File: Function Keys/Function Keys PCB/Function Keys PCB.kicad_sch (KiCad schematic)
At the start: 30 parts, among them J1 Conn_01x05_Female, J2 Conn_01x05_Male

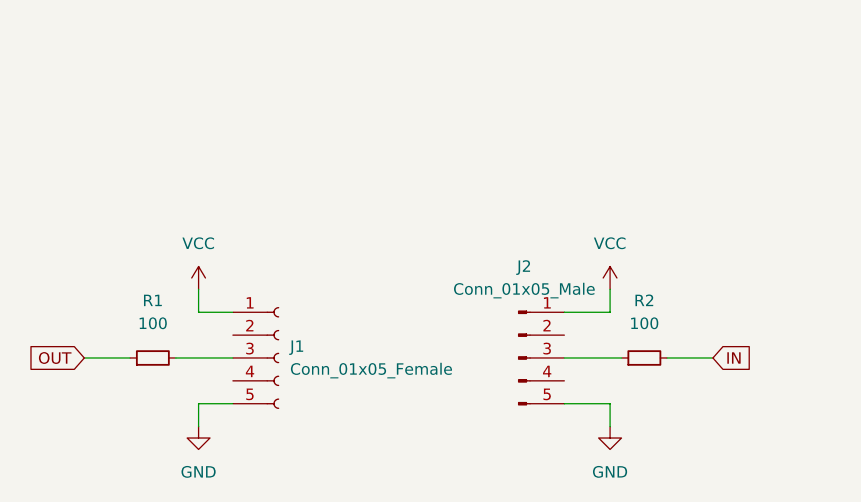
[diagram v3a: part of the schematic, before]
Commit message: Updated connectors
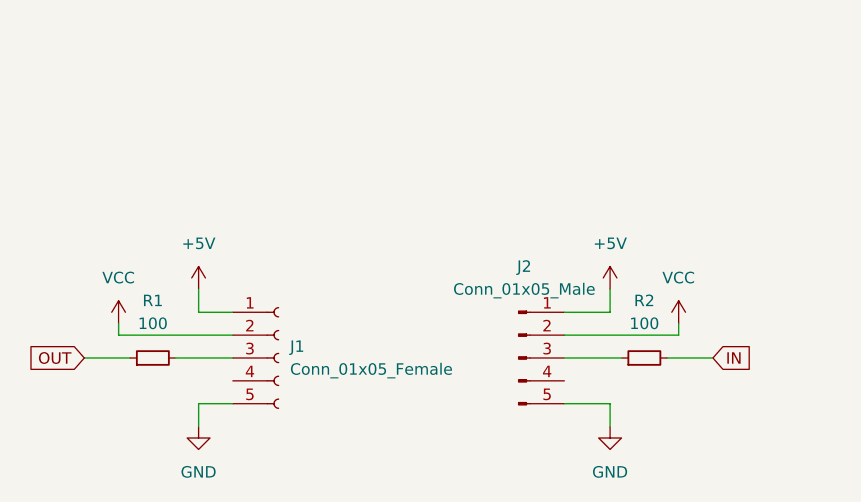
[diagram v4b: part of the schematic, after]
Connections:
- net VCC: now also J1.2 (Pin_2), J2.2 (Pin_2); no longer J1.1 (Pin_1), J2.1 (Pin_1)
- new net +5V: J1.1 (Pin_1), J2.1 (Pin_1)
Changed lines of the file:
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@@
+    (stroke (width 0) (type default) (color 0 0 0 0))
+  )
+  (wire (pts (xy 132.08 133.35) (xy 132.08 134.62))
     (stroke (width 0) (type default) (color 0 0 0 0))
   )
@@
     (stroke (width 0) (type default) (color 0 0 0 0))
   )
+  (wire (pts (xy 119.38 134.62) (xy 132.08 134.62))
+    (stroke (width 0) (type default) (color 0 0 0 0))
+  )
   (wire (pts (xy 176.53 73.66) (xy 176.53 74.93))
     (stroke (width 0) (type default) (color 0 0 0 0))
@@
     (stroke (width 0) (type default) (color 0 0 0 0))
   )
+  (wire (pts (xy 82.55 134.62) (xy 69.85 134.62))
+    (stroke (width 0) (type default) (color 0 0 0 0))
+  )
   (wire (pts (xy 85.09 73.66) (xy 85.09 74.93))
     (stroke (width 0) (type default) (color 0 0 0 0))
@@
   )
   (wire (pts (xy 193.04 72.39) (xy 193.04 73.66))
+    (stroke (width 0) (type default) (color 0 0 0 0))
+  )
+  (wire (pts (xy 69.85 134.62) (xy 69.85 133.35))
     (stroke (width 0) (type default) (color 0 0 0 0))
   )
@@
     (pin "2")
   )
+  (symbol (lib_id "power:+5V") (at 124.46 129.54 0) (unit 1)
+    (in_bom yes) (on_board yes) (fields_autoplaced)
+    (property "Reference" "#PWR?" (id 0) (at 124.46 133.35 0)
+      (effects (font (size 1.27 1.27)) hide)
+    )
+    (property "Value" "+5V" (id 1) (at 124.46 124.46 0))
+    (property "Footprint" "" (id 2) (at 124.46 129.54 0)
+      (effects (font (size 1.27 1.27)) hide)
+    )
+    (property "Datasheet" "" (id 3) (at 124.46 129.54 0)
+      (effects (font (size 1.27 1.27)) hide)
+    )
+    (pin "1")
+  )
   (symbol (lib_id "Connector:Conn_01x05_Male") (at 114.3 137.16 0) (unit 1)
     (in_bom yes) (on_board yes) (fields_autoplaced)
@@
     (pin "2")
   )
+  (symbol (lib_id "power:+5V") (at 78.74 129.54 0) (unit 1)
+    (in_bom yes) (on_board yes) (fields_autoplaced)
+    (property "Reference" "#PWR?" (id 0) (at 78.74 133.35 0)
+      (effects (font (size 1.27 1.27)) hide)
+    )
+    (property "Value" "+5V" (id 1) (at 78.74 124.46 0))
+    (property "Footprint" "" (id 2) (at 78.74 129.54 0)
+      (effects (font (size 1.27 1.27)) hide)
+    )
+    (property "Datasheet" "" (id 3) (at 78.74 129.54 0)
+      (effects (font (size 1.27 1.27)) hide)
+    )
+    (pin "1")
+  )
   (symbol (lib_id "MX_Alps_Hybrid:MX-NoLED") (at 114.3 68.58 0) (unit 1)
     (in_bom yes) (on_board yes) (fields_autoplaced)
@@
     (pin "1")
   )
-  (symbol (lib_id "power:VCC") (at 124.46 129.54 0) (unit 1)
-    (in_bom yes) (on_board yes) (fields_autoplaced)
-    (property "Reference" "#PWR0103" (id 0) (at 124.46 133.35 0)
-      (effects (font (size 1.27 1.27)) hide)
-    )
-    (property "Value" "VCC" (id 1) (at 124.46 124.46 0))
-    (property "Footprint" "" (id 2) (at 124.46 129.54 0)
-      (effects (font (size 1.27 1.27)) hide)
-    )
-    (property "Datasheet" "" (id 3) (at 124.46 129.54 0)
+  (symbol (lib_id "power:VCC") (at 132.08 133.35 0) (unit 1)
+    (in_bom yes) (on_board yes) (fields_autoplaced)
+    (property "Reference" "#PWR0103" (id 0) (at 132.08 137.16 0)
+      (effects (font (size 1.27 1.27)) hide)
+    )
+    (property "Value" "VCC" (id 1) (at 132.08 128.27 0))
+    (property "Footprint" "" (id 2) (at 132.08 133.35 0)
+      (effects (font (size 1.27 1.27)) hide)
+    )
+    (property "Datasheet" "" (id 3) (at 132.08 133.35 0)
       (effects (font (size 1.27 1.27)) hide)
     )
@@
     (pin "2")
   )
-  (symbol (lib_id "power:VCC") (at 78.74 129.54 0) (unit 1)
-    (in_bom yes) (on_board yes) (fields_autoplaced)
-    (property "Reference" "#PWR0101" (id 0) (at 78.74 133.35 0)
-      (effects (font (size 1.27 1.27)) hide)
-    )
-    (property "Value" "VCC" (id 1) (at 78.74 124.46 0))
-    (property "Footprint" "" (id 2) (at 78.74 129.54 0)
-      (effects (font (size 1.27 1.27)) hide)
-    )
-    (property "Datasheet" "" (id 3) (at 78.74 129.54 0)
+  (symbol (lib_id "power:VCC") (at 69.85 133.35 0) (unit 1)
+    (in_bom yes) (on_board yes) (fields_autoplaced)
+    (property "Reference" "#PWR0101" (id 0) (at 69.85 137.16 0)
+      (effects (font (size 1.27 1.27)) hide)
+    )
+    (property "Value" "VCC" (id 1) (at 69.85 128.27 0))
+    (property "Footprint" "" (id 2) (at 69.85 133.35 0)
+      (effects (font (size 1.27 1.27)) hide)
+    )
+    (property "Datasheet" "" (id 3) (at 69.85 133.35 0)
       (effects (font (size 1.27 1.27)) hide)
     )
@@
       (reference "#PWR0104") (unit 1) (value "GND") (footprint "")
     )
+    (path "/28d245e6-760a-415c-8769-f01870c1e875"
+      (reference "#PWR?") (unit 1) (value "+5V") (footprint "")
+    )
+    (path "/5bb24290-bf25-4197-9ffe-91096413c919"
+      (reference "#PWR?") (unit 1) (value "+5V") (footprint "")
+    )
     (path "/46d1f41e-732c-44a9-93bc-50d3da3c5e1f"

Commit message: Updated connector
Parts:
- removed J1: Conn_01x05_Female, Connector_JST:JST_PH_B5B-PH-K_1x05_P2.00mm_Vertical, symbol Connector:Conn_01x05_Female
- removed J2: Conn_01x05_Male, Connector_JST:JST_PH_B5B-PH-K_1x05_P2.00mm_Vertical, symbol Connector:Conn_01x05_Male
- removed R1, R2: 100, Resistor_SMD:R_0805_2012Metric, symbol Device:R_Small
- added J?: Conn_01x18_Male, symbol Connector:Conn_01x18_Male
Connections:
- net +5V: now also J?.1 (Pin_1)
- net COL0: now also J?.3 (Pin_3)
- net COL1: now also J?.4 (Pin_4)
- net COL10: now also J?.13 (Pin_13)
- net COL11: now also J?.14 (Pin_14)
- net COL12: now also J?.15 (Pin_15)
- net COL2: now also J?.5 (Pin_5)
- net COL3: now also J?.6 (Pin_6)
- net COL4: now also J?.7 (Pin_7)
- net COL5: now also J?.8 (Pin_8)
- net COL6: now also J?.9 (Pin_9)
- net COL7: now also J?.10 (Pin_10)
- net COL8: now also J?.11 (Pin_11)
- net COL9: now also J?.12 (Pin_12)
- net GND: now also J?.18 (Pin_18)
- net VCC: now also J?.2 (Pin_2)
- net ROW0 renamed ROW10
- net ROW10: now also J?.17 (Pin_17)
- new net COL13: J?.16 (Pin_16)
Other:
- moved on the sheet: D1, D10, D11, D12, D13, D2, D3, D4, D5, D6, D7, D8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

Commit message: Updated footprints
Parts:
- J1: renamed from J?; footprint (none) -> Connector_JST:JST_SH_SM20B-SRSS-TB_1x20-1MP_P1.00mm_Horizontal
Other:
- note added: "JST Connector"
- note added: "Keycaps"
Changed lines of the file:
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@@
     (stroke (width 0) (type default) (color 0 0 0 0))
+  )
+  (text "Keycaps" (at 107.95 24.13 0)
+    (effects (font (size 2.5 2.5) (thickness 0.5) bold) (justify left bottom))
+  )
+  (text "JST Connector" (at 238.76 22.86 0)
+    (effects (font (size 2.5 2.5) bold) (justify left bottom))
   )
   (global_label "COL9" (shape input) (at 168.91 45.085 90) (fields_autoplaced)
@@
   (symbol (lib_id "power:+5V") (at 256.54 33.655 0) (unit 1)
     (in_bom yes) (on_board yes) (fields_autoplaced)
-    (property "Reference" "#PWR?" (id 0) (at 256.54 37.465 0)
+    (property "Reference" "#PWR0101" (id 0) (at 256.54 37.465 0)
       (effects (font (size 1.27 1.27)) hide)
     )
@@
   (symbol (lib_id "Connector:Conn_01x18_Male") (at 246.38 56.515 0) (unit 1)
     (in_bom yes) (on_board yes) (fields_autoplaced)
-    (property "Reference" "J?" (id 0) (at 247.015 31.115 0))
+    (property "Reference" "J1" (id 0) (at 247.015 31.115 0))
     (property "Value" "Conn_01x18_Male" (id 1) (at 247.015 33.655 0))
-    (property "Footprint" "" (id 2) (at 246.38 56.515 0)
+    (property "Footprint" "Connector_JST:JST_SH_SM20B-SRSS-TB_1x20-1MP_P1.00mm_Horizontal" (id 2) (at 246.38 56.515 0)
       (effects (font (size 1.27 1.27)) hide)
     )
@@
   )
   (symbol_instances
+    (path "/28d245e6-760a-415c-8769-f01870c1e875"
+      (reference "#PWR0101") (unit 1) (value "+5V") (footprint "")
+    )
     (path "/e996d610-320b-458b-b04b-0312af11e60f"
       (reference "#PWR0103") (unit 1) (value "VCC") (footprint "")
@@
       (reference "#PWR0104") (unit 1) (value "GND") (footprint "")
     )
-    (path "/28d245e6-760a-415c-8769-f01870c1e875"
-      (reference "#PWR?") (unit 1) (value "+5V") (footprint "")
-    )
     (path "/46d1f41e-732c-44a9-93bc-50d3da3c5e1f"
       (reference "D1") (unit 1) (value "D_Small") (footprint "Diode_SMD:D_SOD-123")
@@
     )
     (path "/bc8068e2-9f72-4917-94ba-efea6f50fd73"
-      (reference "J?") (unit 1) (value "Conn_01x18_Male") (footprint "")
+      (reference "J1") (unit 1) (value "Conn_01x18_Male") (footprint "Connector_JST:JST_SH_SM20B-SRSS-TB_1x20-1MP_P1.00mm_Horizontal")
     )
     (path "/953e6a73-9071-4c3b-9621-8aa02821bfc7"

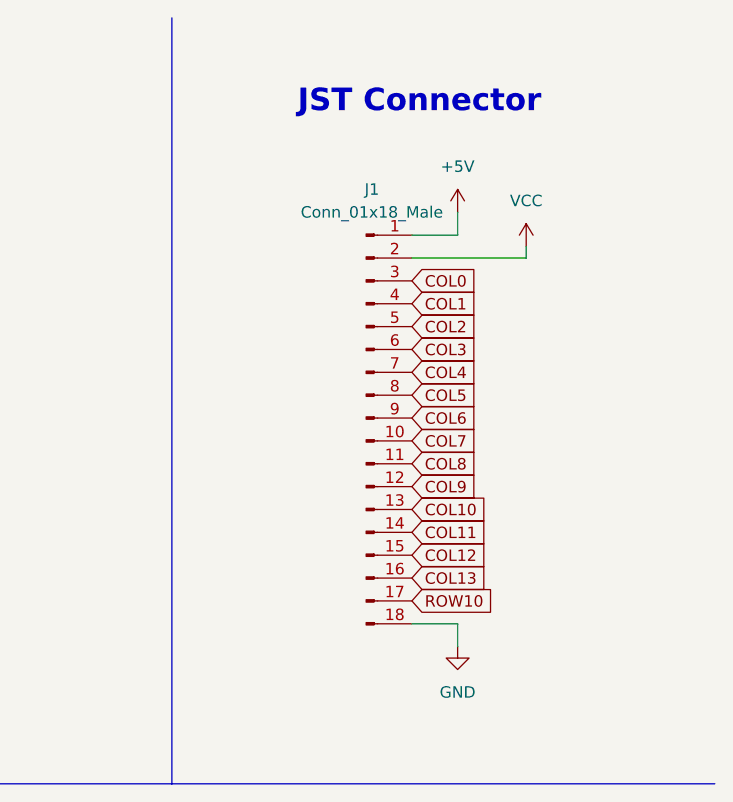
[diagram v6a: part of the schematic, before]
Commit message: Updated connectors and added through holes
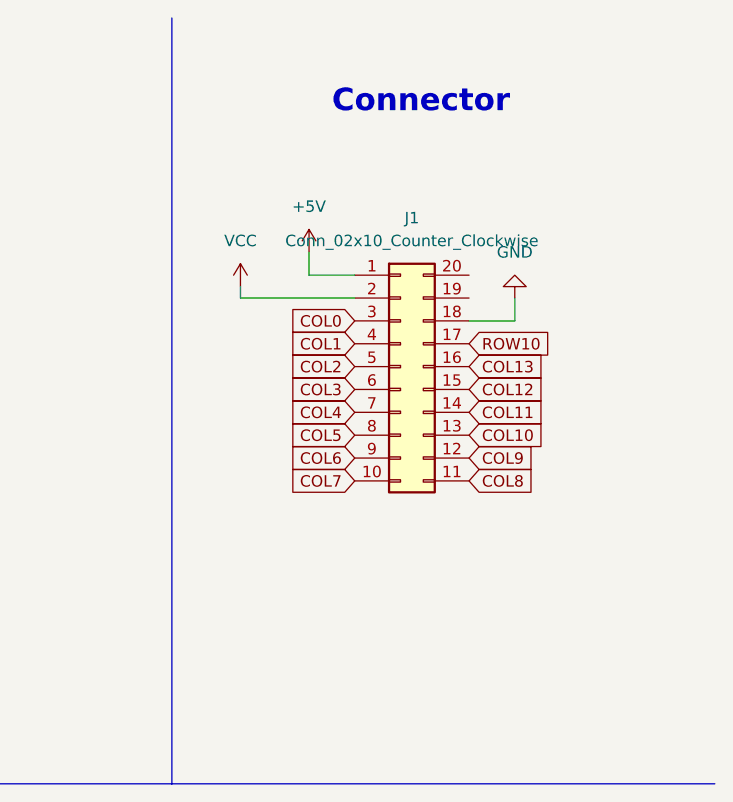
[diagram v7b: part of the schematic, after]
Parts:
- removed J1: Conn_01x18_Male, Connector_JST:JST_SH_SM20B-SRSS-TB_1x20-1MP_P1.00mm_Horizontal, symbol Connector:Conn_01x18_Male
- added J1: Conn_02x10_Counter_Clockwise, Connector_PinHeader_2.54mm:PinHeader_2x10_P2.54mm_Horizontal, symbol Connector_Generic:Conn_02x10_Counter_Clockwise
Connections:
- net +5V: now also J1.1 (Pin_1)
- net COL0: now also J1.3 (Pin_3)
- net COL1: now also J1.4 (Pin_4)
- net COL10: now also J1.13 (Pin_13)
- net COL11: now also J1.14 (Pin_14)
- net COL12: now also J1.15 (Pin_15)
- net COL13: now also J1.16 (Pin_16)
- net COL2: now also J1.5 (Pin_5)
- net COL3: now also J1.6 (Pin_6)
- net COL4: now also J1.7 (Pin_7)
- net COL5: now also J1.8 (Pin_8)
- net COL6: now also J1.9 (Pin_9)
- net COL7: now also J1.10 (Pin_10)
- net COL8: now also J1.11 (Pin_11)
- net COL9: now also J1.12 (Pin_12)
- net GND: now also J1.18 (Pin_18)
- net ROW10: now also J1.17 (Pin_17)
- net VCC: now also J1.2 (Pin_2)
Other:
- note added: "Connector"
- note removed: "JST Connector"

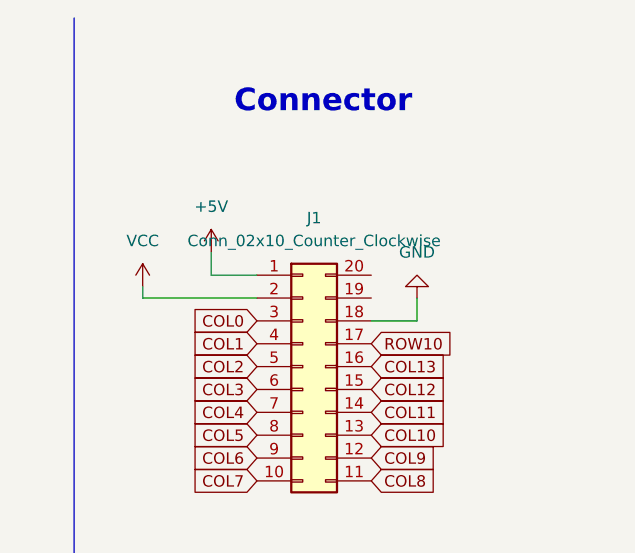
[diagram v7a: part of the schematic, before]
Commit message: Lengthened board & moved ground pin
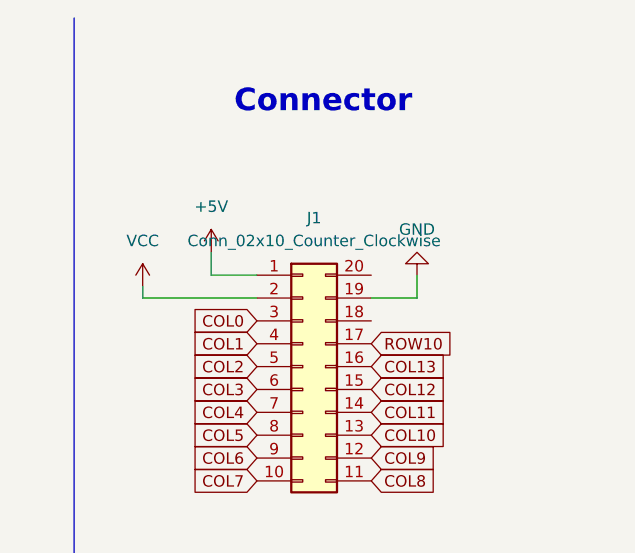
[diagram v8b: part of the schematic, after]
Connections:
- net GND: now also J1.19 (Pin_19); no longer J1.18 (Pin_18)
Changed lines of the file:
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@@
     (stroke (width 0) (type default) (color 0 0 0 0))
   )
-  (wire (pts (xy 262.89 43.18) (xy 262.89 45.72))
+  (wire (pts (xy 262.89 40.64) (xy 262.89 43.18))
     (stroke (width 0) (type default) (color 0 0 0 0))
   )
@@
     (stroke (width 0) (type default) (color 0 0 0 0))
   )
-  (wire (pts (xy 262.89 45.72) (xy 257.81 45.72))
+  (wire (pts (xy 262.89 43.18) (xy 257.81 43.18))
     (stroke (width 0) (type default) (color 0 0 0 0))
   )
@@
     (pin "2")
   )
-  (symbol (lib_id "power:GND") (at 262.89 43.18 180) (unit 1)
-    (in_bom yes) (on_board yes) (fields_autoplaced)
-    (property "Reference" "#PWR0104" (id 0) (at 262.89 36.83 0)
-      (effects (font (size 1.27 1.27)) hide)
-    )
-    (property "Value" "GND" (id 1) (at 262.89 38.1 0))
-    (property "Footprint" "" (id 2) (at 262.89 43.18 0)
-      (effects (font (size 1.27 1.27)) hide)
-    )
-    (property "Datasheet" "" (id 3) (at 262.89 43.18 0)
-      (effects (font (size 1.27 1.27)) hide)
-    )
+  (symbol (lib_id "power:GND") (at 262.89 40.64 180) (unit 1)
+    (in_bom yes) (on_board yes) (fields_autoplaced)
+    (property "Reference" "#PWR0104" (id 0) (at 262.89 34.29 0)
+      (effects (font (size 1.27 1.27)) hide)
+    )
+    (property "Value" "GND" (id 1) (at 262.89 35.56 0))
+    (property "Footprint" "" (id 2) (at 262.89 40.64 0)
+      (effects (font (size 1.27 1.27)) hide)
+    )
+    (property "Datasheet" "" (id 3) (at 262.89 40.64 0)
+      (effects (font (size 1.27 1.27)) hide)
+    )
